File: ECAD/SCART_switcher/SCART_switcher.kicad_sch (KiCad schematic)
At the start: 8 parts

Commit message: progressed ecad
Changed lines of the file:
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@@
   (bus_alias "SOURCE_STATUS" (members "IN1_ACTIVE" "IN2_ACTIVE" "IN3_ACTIVE" "IN4_ACTIVE" "IN5_ACTIVE" "IN6_ACTIVE" "IN7_ACTIVE" "IN8_ACTIVE" "IN9_ACTIVE" "IN10_ACTIVE"))
   (bus_alias "VIDEO_SIGNALS" (members "RED" "BLUE" "GREEN" "VIDEO/RGB_SYNC" "BLANKING" "AUDIO_LEFT" "AUDIO_RIGHT"))
-  (junction (at 162.56 46.99) (diameter 0) (color 0 0 0 0)
-  )
   (junction (at 162.56 78.74) (diameter 0) (color 0 0 0 0)
   )
+  (junction (at 162.56 39.37) (diameter 0) (color 0 0 0 0)
+  )
   (junction (at 95.25 187.96) (diameter 0) (color 0 0 0 0)
   )
   (junction (at 246.38 81.28) (diameter 0) (color 0 0 0 0)
   )
-  (junction (at 166.37 116.84) (diameter 0) (color 0 0 0 0)
+  (junction (at 166.37 118.11) (diameter 0) (color 0 0 0 0)
   )
   (bus_entry (at 95.25 158.75) (size 2.54 -2.54)
@@
     (stroke (width 0) (type default))
   )
-  (bus (pts (xy 162.56 46.99) (xy 190.5 46.99))
+  (bus (pts (xy 162.56 39.37) (xy 190.5 39.37))
     (stroke (width 0) (type default))
   )
@@
     (stroke (width 0) (type default))
   )
-  (bus (pts (xy 162.56 46.99) (xy 162.56 53.34))
-    (stroke (width 0) (type default))
-  )
   (bus (pts (xy 83.82 151.13) (xy 83.82 153.67))
     (stroke (width 0) (type default))
@@
     (stroke (width 0) (type default))
   )
-  (bus (pts (xy 166.37 107.95) (xy 166.37 116.84))
-    (stroke (width 0) (type default))
-  )
   (wire (pts (xy 160.02 73.6349) (xy 154.6885 73.6349))
     (stroke (width 0) (type default))
@@
     (stroke (width 0) (type default))
   )
-  (bus (pts (xy 166.37 116.84) (xy 166.37 139.7))
+  (bus (pts (xy 166.37 107.95) (xy 166.37 118.11))
     (stroke (width 0) (type default))
   )
@@
     (stroke (width 0) (type default))
   )
-  (bus (pts (xy 173.99 121.92) (xy 257.81 121.92))
+  (bus (pts (xy 173.99 125.73) (xy 257.81 125.73))
     (stroke (width 0) (type default))
   )
@@
     (stroke (width 0) (type default))
   )
-  (bus (pts (xy 257.81 118.11) (xy 257.81 121.92))
+  (bus (pts (xy 257.81 118.11) (xy 257.81 125.73))
     (stroke (width 0) (type default))
   )
@@
     (stroke (width 0) (type default))
   )
-  (bus (pts (xy 162.56 36.83) (xy 162.56 46.99))
+  (bus (pts (xy 162.56 36.83) (xy 162.56 39.37))
     (stroke (width 0) (type default))
   )
@@
     (stroke (width 0) (type default))
   )
-  (bus (pts (xy 166.37 116.84) (xy 191.77 116.84))
+  (bus (pts (xy 166.37 118.11) (xy 191.77 118.11))
     (stroke (width 0) (type default))
   )
@@
     (stroke (width 0) (type default))
   )
-  (bus (pts (xy 173.99 121.92) (xy 173.99 187.96))
+  (bus (pts (xy 173.99 125.73) (xy 173.99 187.96))
     (stroke (width 0) (type default))
   )
@@
     (stroke (width 0) (type default))
   )
-  (bus (pts (xy 191.77 115.57) (xy 191.77 116.84))
+  (bus (pts (xy 191.77 115.57) (xy 191.77 118.11))
     (stroke (width 0) (type default))
   )
@@
     (stroke (width 0) (type default))
   )
+  (bus (pts (xy 166.37 118.11) (xy 166.37 139.7))
+    (stroke (width 0) (type default))
+  )
   (wire (pts (xy 142.24 87.63) (xy 160.02 87.63))
     (stroke (width 0) (type default))
@@
     (stroke (width 0) (type default))
   )
-  (bus (pts (xy 190.5 36.83) (xy 190.5 46.99))
+  (bus (pts (xy 190.5 36.83) (xy 190.5 39.37))
     (stroke (width 0) (type default))
   )
@@
     (stroke (width 0) (type default))
   )
+  (bus (pts (xy 162.56 39.37) (xy 162.56 53.34))
+    (stroke (width 0) (type default))
+  )

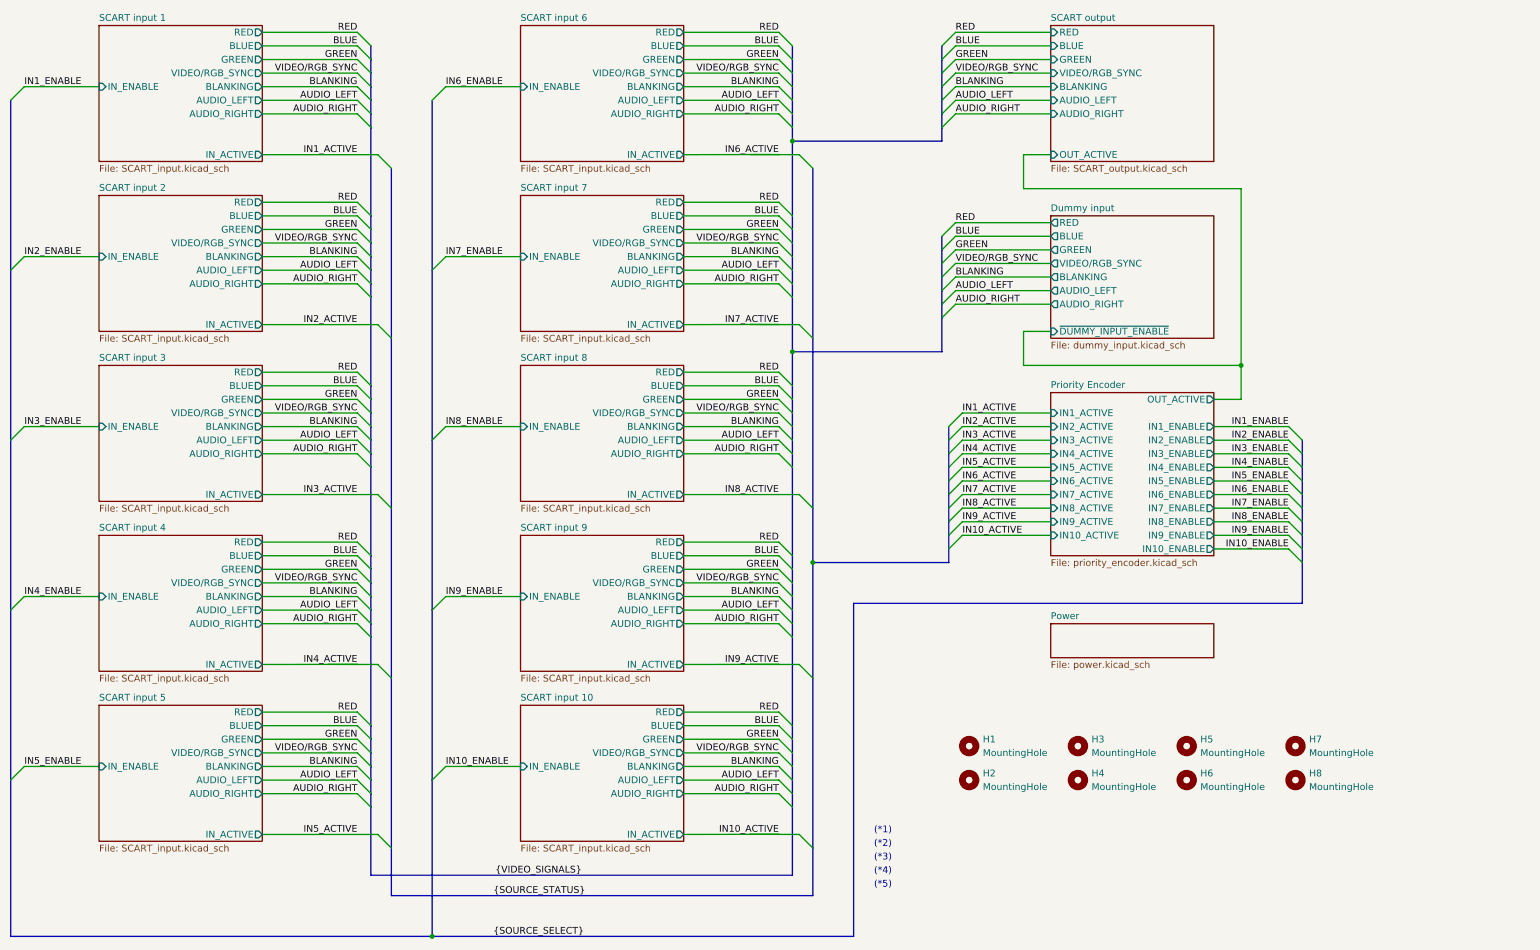
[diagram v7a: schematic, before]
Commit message: ERC fixes.
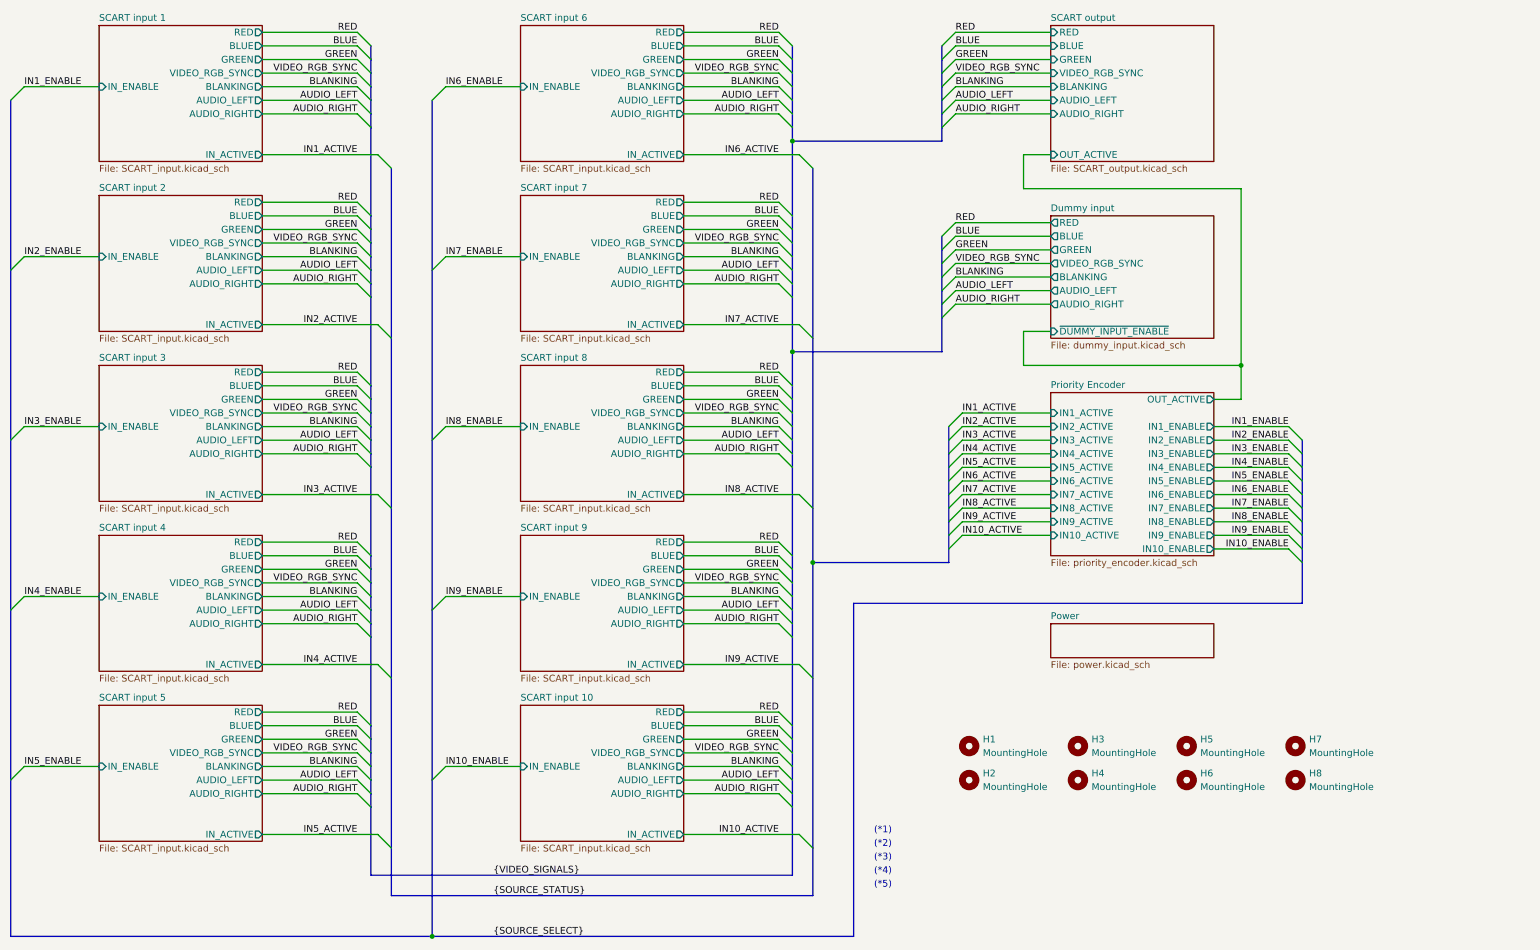
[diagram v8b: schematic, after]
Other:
- sheet Dummy input ports: added VIDEO_RGB_SYNC; removed VIDEO/RGB_SYNC
- sheet SCART input 1 ports: added VIDEO_RGB_SYNC; removed VIDEO/RGB_SYNC
- sheet SCART input 10 ports: added VIDEO_RGB_SYNC; removed VIDEO/RGB_SYNC
- sheet SCART input 2 ports: added VIDEO_RGB_SYNC; removed VIDEO/RGB_SYNC
- sheet SCART input 3 ports: added VIDEO_RGB_SYNC; removed VIDEO/RGB_SYNC
- sheet SCART input 4 ports: added VIDEO_RGB_SYNC; removed VIDEO/RGB_SYNC
- sheet SCART input 5 ports: added VIDEO_RGB_SYNC; removed VIDEO/RGB_SYNC
- sheet SCART input 6 ports: added VIDEO_RGB_SYNC; removed VIDEO/RGB_SYNC
- sheet SCART input 7 ports: added VIDEO_RGB_SYNC; removed VIDEO/RGB_SYNC
- sheet SCART input 8 ports: added VIDEO_RGB_SYNC; removed VIDEO/RGB_SYNC
- sheet SCART input 9 ports: added VIDEO_RGB_SYNC; removed VIDEO/RGB_SYNC
- sheet SCART output ports: added VIDEO_RGB_SYNC; removed VIDEO/RGB_SYNC
